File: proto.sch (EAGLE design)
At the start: 2 parts

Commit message: schematic terminada, creo que decente
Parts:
- added JP1, JP2, JP3: (no value), pinhead:PINHD-1X3
- added JP4: (no value), pinhead:PINHD-1X2
- added X1: 87758-1216, con-molex:87758-1216
- added X2: 87758-0416, con-molex:87758-0416
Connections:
- removed net N$8: TB1.VCC, U$1.3.3V
- new net N$12: TB1.A2, X2-2.S
- new net N$13: TB1.B2, X2-4.S
- new net N$14: TB1.B1, X2-3.S
- new net N$15: TB1.A1, X2-1.S
- new net N$17: JP1.2, U$1.A7
- new net N$18: U$1.3.3V, X1-9.S
- new net N$19: U$1.A5, X1-2.S
- new net N$20: U$1.A4, X1-4.S
- new net N$21: U$1.A3, X1-12.S
- new net N$24: U$1.A0, X1-6.S
- new net N$25: JP1.1, JP2.1, JP3.1, JP4.2, TB1.GND2, U$1.GND, X1-1.S
- new net N$26: JP2.2, JP3.2, U$1.A6
- new net N$27: JP1.3, JP2.3, JP3.3, TB1.VCC, U$1.5.5V
- new net N$28: U$1.A2, X1-10.S
- new net N$29: U$1.A1, X1-8.S
- net N$9: now also JP4.1

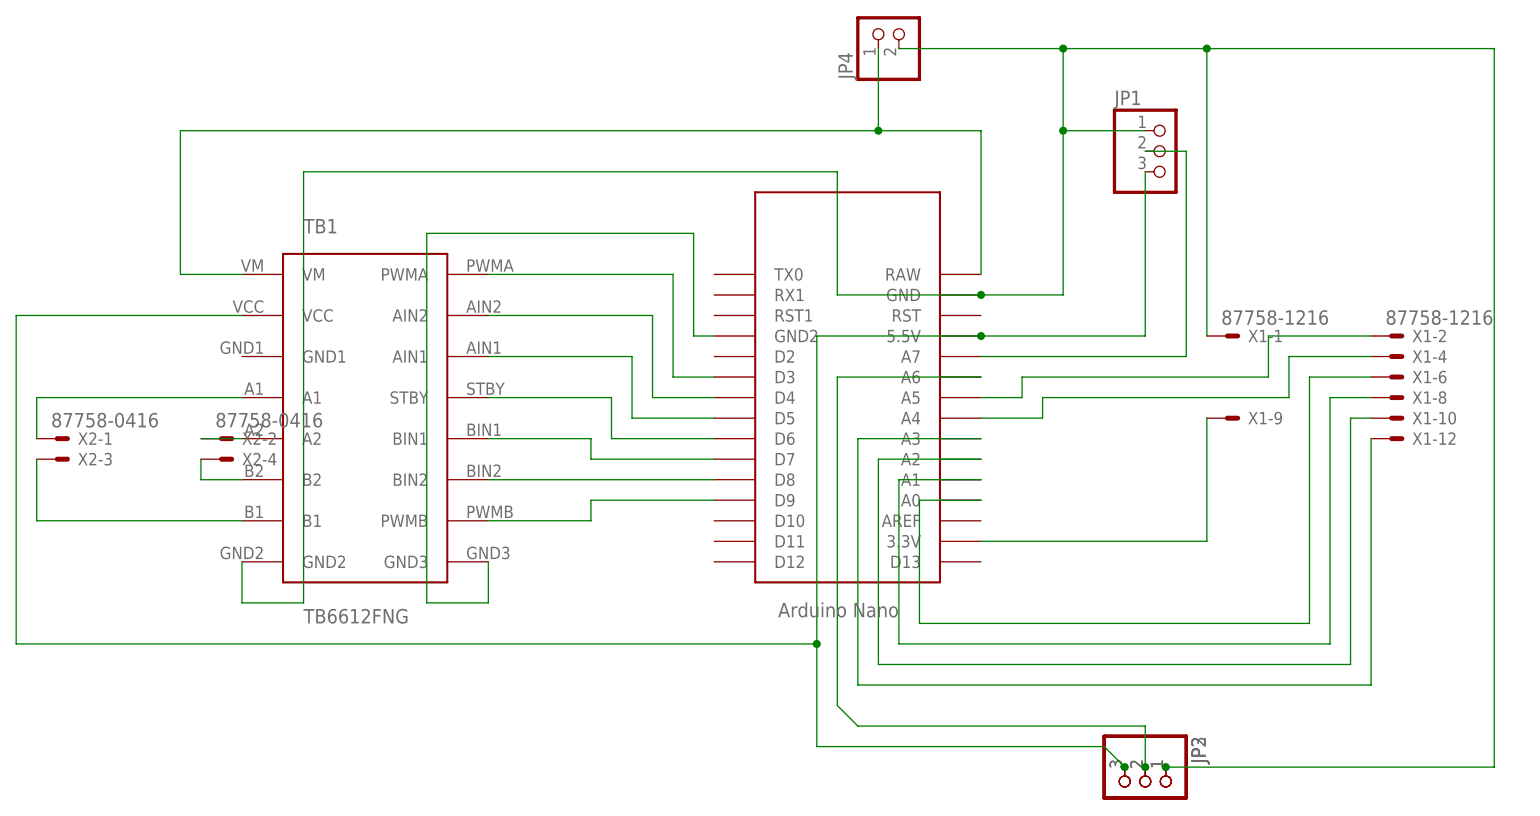
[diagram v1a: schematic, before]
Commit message: finished schematic
last one didn't use the correct pins
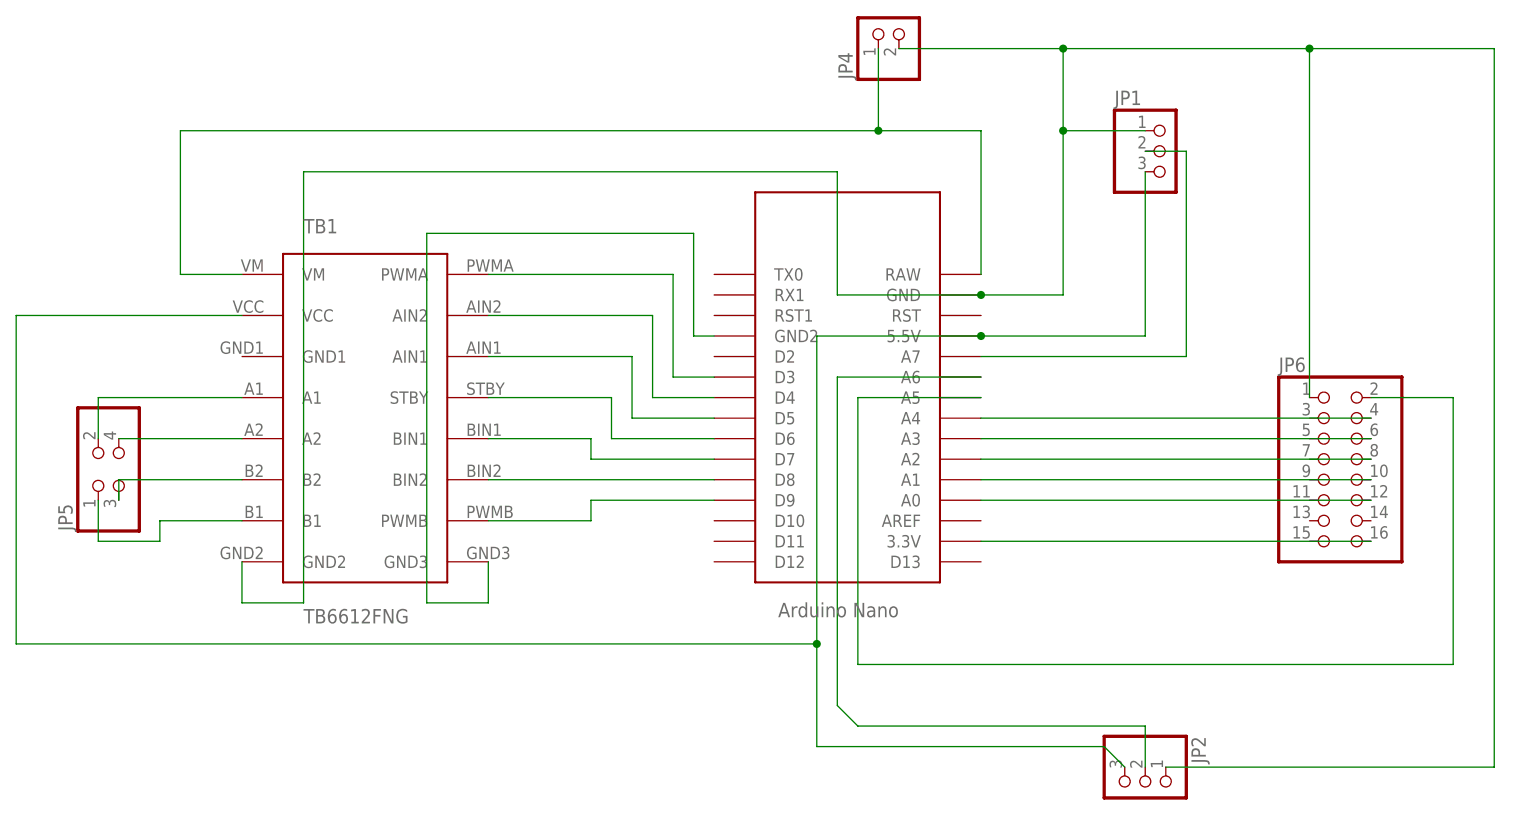
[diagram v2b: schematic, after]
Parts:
- removed JP3: (no value), pinhead:PINHD-1X3
- removed X1: 87758-1216, con-molex:87758-1216
- removed X2: 87758-0416, con-molex:87758-0416
- added JP5: (no value), pinhead:PINHD-2X2
- added JP6: (no value), pinhead:PINHD-2X8
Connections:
- removed net N$24: U$1.A0, X1-6.S
- removed net N$28: U$1.A2, X1-10.S
- removed net N$29: U$1.A1, X1-8.S
- new net N$11: JP5.4, TB1.A2
- new net N$16: JP6.10, U$1.A1
- new net N$8: JP5.2, TB1.A1
- net N$12: now also JP5.3, TB1.B2; no longer TB1.A2, X2-2.S
- net N$13: now also JP5.1, TB1.B1; no longer TB1.B2, X2-4.S
- net N$14: now also JP6.16, U$1.3.3V; no longer TB1.B1, X2-3.S
- net N$15: now also JP6.12, U$1.A0; no longer TB1.A1, X2-1.S
- net N$18: now also JP6.8, U$1.A2; no longer U$1.3.3V, X1-9.S
- net N$19: now also JP6.6, U$1.A3; no longer U$1.A5, X1-2.S
- net N$20: now also JP6.4; no longer X1-4.S
- net N$21: now also JP6.2, U$1.A5; no longer U$1.A3, X1-12.S
- net N$25: now also JP6.1; no longer JP3.1, X1-1.S
- net N$26: no longer JP3.2
- net N$27: no longer JP3.3

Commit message: eliminar tierras
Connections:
- removed net N$10: TB1.GND3, U$1.GND2
- removed net N$25: JP1.1, JP2.1, JP4.2, JP6.1, TB1.GND2, U$1.GND
- net N$14: now also JP6.15
- net N$15: now also JP6.11
- net N$16: now also JP6.9
- net N$18: now also JP6.7
- net N$19: now also JP6.5
- net N$20: now also JP6.3
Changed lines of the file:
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@@
-</segment>
-</net>
-<net name="N$10" class="0">
-<segment>
-<pinref part="U$1" gate="G$1" pin="GND2"/>
-<wire x1="132.08" y1="-22.86" x2="129.54" y2="-22.86" width="0.1524" layer="91"/>
-<wire x1="129.54" y1="-22.86" x2="129.54" y2="-10.16" width="0.1524" layer="91"/>
-<wire x1="129.54" y1="-10.16" x2="96.52" y2="-10.16" width="0.1524" layer="91"/>
-<wire x1="96.52" y1="-10.16" x2="96.52" y2="-55.88" width="0.1524" layer="91"/>
-<wire x1="96.52" y1="-55.88" x2="104.14" y2="-55.88" width="0.1524" layer="91"/>
-<pinref part="TB1" gate="G$1" pin="GND3"/>
-<wire x1="104.14" y1="-55.88" x2="104.14" y2="-50.8" width="0.1524" layer="91"/>
 </segment>
 </net>
@@
 <wire x1="190.5" y1="0" x2="190.5" y2="-25.4" width="0.1524" layer="91"/>
 <wire x1="190.5" y1="-25.4" x2="165.1" y2="-25.4" width="0.1524" layer="91"/>
-</segment>
-</net>
-<net name="N$25" class="0">
-<segment>
-<wire x1="187.96" y1="-76.2" x2="228.6" y2="-76.2" width="0.1524" layer="91"/>
-<pinref part="U$1" gate="G$1" pin="GND"/>
-<wire x1="165.1" y1="-17.78" x2="147.32" y2="-17.78" width="0.1524" layer="91"/>
-<wire x1="147.32" y1="-17.78" x2="147.32" y2="-2.54" width="0.1524" layer="91"/>
-<wire x1="147.32" y1="-2.54" x2="81.28" y2="-2.54" width="0.1524" layer="91"/>
-<wire x1="81.28" y1="-2.54" x2="81.28" y2="-55.88" width="0.1524" layer="91"/>
-<wire x1="81.28" y1="-55.88" x2="73.66" y2="-55.88" width="0.1524" layer="91"/>
-<pinref part="TB1" gate="G$1" pin="GND2"/>
-<wire x1="73.66" y1="-55.88" x2="73.66" y2="-50.8" width="0.1524" layer="91"/>
-<pinref part="JP1" gate="A" pin="1"/>
-<wire x1="185.42" y1="2.54" x2="175.26" y2="2.54" width="0.1524" layer="91"/>
-<wire x1="175.26" y1="2.54" x2="175.26" y2="-17.78" width="0.1524" layer="91"/>
-<wire x1="175.26" y1="-17.78" x2="165.1" y2="-17.78" width="0.1524" layer="91"/>
-<junction x="165.1" y="-17.78"/>
-<wire x1="228.6" y1="-76.2" x2="228.6" y2="12.7" width="0.1524" layer="91"/>
-<wire x1="228.6" y1="12.7" x2="205.74" y2="12.7" width="0.1524" layer="91"/>
-<wire x1="205.74" y1="12.7" x2="175.26" y2="12.7" width="0.1524" layer="91"/>
-<wire x1="175.26" y1="12.7" x2="175.26" y2="2.54" width="0.1524" layer="91"/>
-<junction x="175.26" y="2.54"/>
-<pinref part="JP4" gate="G$1" pin="2"/>
-<wire x1="154.94" y1="12.7" x2="175.26" y2="12.7" width="0.1524" layer="91"/>
-<junction x="175.26" y="12.7"/>
-<pinref part="JP6" gate="A" pin="1"/>
-<wire x1="205.74" y1="-30.48" x2="205.74" y2="12.7" width="0.1524" layer="91"/>
-<junction x="205.74" y="12.7"/>
-<pinref part="JP2" gate="A" pin="1"/>
 </segment>
 </net>
@@
 <pinref part="JP6" gate="A" pin="16"/>
 <pinref part="U$1" gate="G$1" pin="3.3V"/>
-<wire x1="213.36" y1="-48.26" x2="165.1" y2="-48.26" width="0.1524" layer="91"/>
+<wire x1="213.36" y1="-48.26" x2="205.74" y2="-48.26" width="0.1524" layer="91"/>
+<pinref part="JP6" gate="A" pin="15"/>
+<wire x1="205.74" y1="-48.26" x2="165.1" y2="-48.26" width="0.1524" layer="91"/>
+<junction x="205.74" y="-48.26"/>
 </segment>
 </net>
@@
 <pinref part="JP6" gate="A" pin="12"/>
 <pinref part="U$1" gate="G$1" pin="A0"/>
-<wire x1="213.36" y1="-43.18" x2="165.1" y2="-43.18" width="0.1524" layer="91"/>
+<wire x1="213.36" y1="-43.18" x2="205.74" y2="-43.18" width="0.1524" layer="91"/>
+<pinref part="JP6" gate="A" pin="11"/>
+<wire x1="205.74" y1="-43.18" x2="165.1" y2="-43.18" width="0.1524" layer="91"/>
+<junction x="205.74" y="-43.18"/>
 </segment>
 </net>
@@
 <pinref part="JP6" gate="A" pin="10"/>
 <pinref part="U$1" gate="G$1" pin="A1"/>
-<wire x1="213.36" y1="-40.64" x2="165.1" y2="-40.64" width="0.1524" layer="91"/>
+<wire x1="213.36" y1="-40.64" x2="205.74" y2="-40.64" width="0.1524" layer="91"/>
+<pinref part="JP6" gate="A" pin="9"/>
+<wire x1="205.74" y1="-40.64" x2="165.1" y2="-40.64" width="0.1524" layer="91"/>
+<junction x="205.74" y="-40.64"/>
 </segment>
 </net>
@@
 <pinref part="JP6" gate="A" pin="8"/>
 <pinref part="U$1" gate="G$1" pin="A2"/>
-<wire x1="213.36" y1="-38.1" x2="165.1" y2="-38.1" width="0.1524" layer="91"/>
+<wire x1="213.36" y1="-38.1" x2="205.74" y2="-38.1" width="0.1524" layer="91"/>
+<pinref part="JP6" gate="A" pin="7"/>
+<wire x1="205.74" y1="-38.1" x2="165.1" y2="-38.1" width="0.1524" layer="91"/>
+<junction x="205.74" y="-38.1"/>
 </segment>
 </net>
@@
 <pinref part="JP6" gate="A" pin="6"/>
 <pinref part="U$1" gate="G$1" pin="A3"/>
-<wire x1="213.36" y1="-35.56" x2="165.1" y2="-35.56" width="0.1524" layer="91"/>
+<wire x1="213.36" y1="-35.56" x2="205.74" y2="-35.56" width="0.1524" layer="91"/>
+<pinref part="JP6" gate="A" pin="5"/>
+<wire x1="205.74" y1="-35.56" x2="165.1" y2="-35.56" width="0.1524" layer="91"/>
+<junction x="205.74" y="-35.56"/>
 </segment>
 </net>
@@
 <pinref part="JP6" gate="A" pin="4"/>
 <pinref part="U$1" gate="G$1" pin="A4"/>
-<wire x1="213.36" y1="-33.02" x2="165.1" y2="-33.02" width="0.1524" layer="91"/>
+<wire x1="213.36" y1="-33.02" x2="205.74" y2="-33.02" width="0.1524" layer="91"/>
+<pinref part="JP6" gate="A" pin="3"/>
+<wire x1="205.74" y1="-33.02" x2="165.1" y2="-33.02" width="0.1524" layer="91"/>
+<junction x="205.74" y="-33.02"/>
 </segment>
 </net>

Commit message: holi
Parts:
- removed JP6: (no value), pinhead:PINHD-2X8
- added JP3: (no value), pinhead:PINHD-2X9
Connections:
- removed net N$21: JP6.2, U$1.A5
- new net N$10: JP3.4, U$1.A5
- net N$14: now also JP3.6, U$1.A4; no longer JP6.15, JP6.16, U$1.3.3V
- net N$15: now also JP3.8, U$1.A3; no longer JP6.11, JP6.12, U$1.A0
- net N$16: now also JP3.10, U$1.A2; no longer JP6.10, JP6.9, U$1.A1
- net N$18: now also JP3.12, U$1.A1; no longer JP6.7, JP6.8, U$1.A2
- net N$19: now also JP3.14, U$1.A0; no longer JP6.5, JP6.6, U$1.A3
- net N$20: now also JP3.18, U$1.3.3V; no longer JP6.3, JP6.4, U$1.A4
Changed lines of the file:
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@@
 <setting verticaltext="up"/>
 </settings>
-<grid distance="0.1" unitdist="inch" unit="inch" style="lines" multiple="1" display="yes" altdistance="0.01" altunitdist="inch" altunit="inch"/>
+<grid distance="0.1" unitdist="inch" unit="inch" style="lines" multiple="1" display="no" altdistance="0.01" altunitdist="inch" altunit="inch"/>
 <layers>
 <layer number="1" name="Top" color="4" fill="1" visible="no" active="no"/>
@@
 <part name="JP4" library="pinhead" library_urn="urn:adsk.eagle:library:325" deviceset="PINHD-1X2" device="" package3d_urn="urn:adsk.eagle:package:22435/2"/>
 <part name="JP5" library="pinhead" library_urn="urn:adsk.eagle:library:325" deviceset="PINHD-2X2" device="" package3d_urn="urn:adsk.eagle:package:22455/2"/>
-<part name="JP6" library="pinhead" library_urn="urn:adsk.eagle:library:325" deviceset="PINHD-2X8" device="" package3d_urn="urn:adsk.eagle:package:22481/2"/>
 <part name="JP2" library="pinhead" library_urn="urn:adsk.eagle:library:325" deviceset="PINHD-1X3" device="" package3d_urn="urn:adsk.eagle:package:22458/2"/>
+<part name="JP3" library="pinhead" library_urn="urn:adsk.eagle:library:325" deviceset="PINHD-2X9" device="" package3d_urn="urn:adsk.eagle:package:22484/2"/>
 </parts>
 <sheets>
@@
 <attribute name="VALUE" x="63.5" y="-46.99" size="1.778" layer="96" rot="R90"/>
 </instance>
-<instance part="JP6" gate="A" x="208.28" y="-38.1">
-<attribute name="NAME" x="201.93" y="-27.305" size="1.778" layer="95"/>
-<attribute name="VALUE" x="201.93" y="-53.34" size="1.778" layer="96"/>
-</instance>
 <instance part="JP2" gate="A" x="185.42" y="-78.74" rot="R270">
 <attribute name="NAME" x="191.135" y="-72.39" size="1.778" layer="95" rot="R270"/>
 <attribute name="VALUE" x="177.8" y="-72.39" size="1.778" layer="96" rot="R270"/>
+</instance>
+<instance part="JP3" gate="A" x="208.28" y="-38.1">
+<attribute name="NAME" x="201.93" y="-24.765" size="1.778" layer="95"/>
+<attribute name="VALUE" x="201.93" y="-53.34" size="1.778" layer="96"/>
 </instance>
 </instances>
@@
 </segment>
 </net>
+<net name="N$10" class="0">
+<segment>
+<pinref part="U$1" gate="G$1" pin="A5"/>
+<pinref part="JP3" gate="A" pin="4"/>
+<wire x1="165.1" y1="-30.48" x2="213.36" y2="-30.48" width="0.1524" layer="91"/>
+</segment>
+</net>
 <net name="N$14" class="0">
 <segment>
-<pinref part="JP6" gate="A" pin="16"/>
+<pinref part="U$1" gate="G$1" pin="A4"/>
+<pinref part="JP3" gate="A" pin="6"/>
+<wire x1="165.1" y1="-33.02" x2="213.36" y2="-33.02" width="0.1524" layer="91"/>
+</segment>
+</net>
+<net name="N$15" class="0">
+<segment>
+<pinref part="U$1" gate="G$1" pin="A3"/>
+<pinref part="JP3" gate="A" pin="8"/>
+<wire x1="165.1" y1="-35.56" x2="213.36" y2="-35.56" width="0.1524" layer="91"/>
+</segment>
+</net>
+<net name="N$16" class="0">
+<segment>
+<pinref part="JP3" gate="A" pin="10"/>
+<pinref part="U$1" gate="G$1" pin="A2"/>
+<wire x1="213.36" y1="-38.1" x2="165.1" y2="-38.1" width="0.1524" layer="91"/>
+</segment>
+</net>
+<net name="N$18" class="0">
+<segment>
+<pinref part="U$1" gate="G$1" pin="A1"/>
+<pinref part="JP3" gate="A" pin="12"/>
+<wire x1="165.1" y1="-40.64" x2="213.36" y2="-40.64" width="0.1524" layer="91"/>
+</segment>
+</net>
+<net name="N$19" class="0">
+<segment>
+<pinref part="JP3" gate="A" pin="14"/>
+<pinref part="U$1" gate="G$1" pin="A0"/>
+<wire x1="213.36" y1="-43.18" x2="165.1" y2="-43.18" width="0.1524" layer="91"/>
+</segment>
+</net>
+<net name="N$20" class="0">
+<segment>
 <pinref part="U$1" gate="G$1" pin="3.3V"/>
-<wire x1="213.36" y1="-48.26" x2="205.74" y2="-48.26" width="0.1524" layer="91"/>
-<pinref part="JP6" gate="A" pin="15"/>
-<wire x1="205.74" y1="-48.26" x2="165.1" y2="-48.26" width="0.1524" layer="91"/>
-<junction x="205.74" y="-48.26"/>
-</segment>
-</net>
-<net name="N$15" class="0">
-<segment>
-<pinref part="JP6" gate="A" pin="12"/>
-<pinref part="U$1" gate="G$1" pin="A0"/>
-<wire x1="213.36" y1="-43.18" x2="205.74" y2="-43.18" width="0.1524" layer="91"/>
-<pinref part="JP6" gate="A" pin="11"/>
-<wire x1="205.74" y1="-43.18" x2="165.1" y2="-43.18" width="0.1524" layer="91"/>
-<junction x="205.74" y="-43.18"/>
-</segment>
-</net>
-<net name="N$16" class="0">
-<segment>
-<pinref part="JP6" gate="A" pin="10"/>
-<pinref part="U$1" gate="G$1" pin="A1"/>
-<wire x1="213.36" y1="-40.64" x2="205.74" y2="-40.64" width="0.1524" layer="91"/>
-<pinref part="JP6" gate="A" pin="9"/>
-<wire x1="205.74" y1="-40.64" x2="165.1" y2="-40.64" width="0.1524" layer="91"/>
-<junction x="205.74" y="-40.64"/>
-</segment>
-</net>
-<net name="N$18" class="0">
-<segment>
-<pinref part="JP6" gate="A" pin="8"/>
-<pinref part="U$1" gate="G$1" pin="A2"/>
-<wire x1="213.36" y1="-38.1" x2="205.74" y2="-38.1" width="0.1524" layer="91"/>
-<pinref part="JP6" gate="A" pin="7"/>
-<wire x1="205.74" y1="-38.1" x2="165.1" y2="-38.1" width="0.1524" layer="91"/>
-<junction x="205.74" y="-38.1"/>
-</segment>
-</net>
-<net name="N$19" class="0">
-<segment>
-<pinref part="JP6" gate="A" pin="6"/>
-<pinref part="U$1" gate="G$1" pin="A3"/>
-<wire x1="213.36" y1="-35.56" x2="205.74" y2="-35.56" width="0.1524" layer="91"/>
-<pinref part="JP6" gate="A" pin="5"/>
-<wire x1="205.74" y1="-35.56" x2="165.1" y2="-35.56" width="0.1524" layer="91"/>
-<junction x="205.74" y="-35.56"/>
-</segment>
-</net>
-<net name="N$20" class="0">
-<segment>
-<pinref part="JP6" gate="A" pin="4"/>
-<pinref part="U$1" gate="G$1" pin="A4"/>
-<wire x1="213.36" y1="-33.02" x2="205.74" y2="-33.02" width="0.1524" layer="91"/>
-<pinref part="JP6" gate="A" pin="3"/>
-<wire x1="205.74" y1="-33.02" x2="165.1" y2="-33.02" width="0.1524" layer="91"/>
-<junction x="205.74" y="-33.02"/>
-</segment>
-</net>
-<net name="N$21" class="0">
-<segment>
-<pinref part="JP6" gate="A" pin="2"/>
-<wire x1="213.36" y1="-30.48" x2="223.52" y2="-30.48" width="0.1524" layer="91"/>
-<wire x1="223.52" y1="-30.48" x2="223.52" y2="-63.5" width="0.1524" layer="91"/>
-<wire x1="223.52" y1="-63.5" x2="149.86" y2="-63.5" width="0.1524" layer="91"/>
-<wire x1="149.86" y1="-63.5" x2="149.86" y2="-30.48" width="0.1524" layer="91"/>
-<pinref part="U$1" gate="G$1" pin="A5"/>
-<wire x1="149.86" y1="-30.48" x2="165.1" y2="-30.48" width="0.1524" layer="91"/>
-</segment>
-</net>
+<pinref part="JP3" gate="A" pin="18"/>
+<wire x1="165.1" y1="-48.26" x2="213.36" y2="-48.26" width="0.1524" layer="91"/>
+</segment>
+</net>

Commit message: monton de weas
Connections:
- new net GND: JP1.1, JP2.1, JP3.1, JP4.2, TB1.GND2, TB1.GND3, U$1.GND, U$1.GND2
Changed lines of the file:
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@@
+</segment>
+</net>
+<net name="GND" class="0">
+<segment>
+<pinref part="TB1" gate="G$1" pin="GND2"/>
+<wire x1="73.66" y1="-50.8" x2="73.66" y2="-55.88" width="0.1524" layer="91"/>
+<wire x1="73.66" y1="-55.88" x2="66.04" y2="-55.88" width="0.1524" layer="91"/>
+</segment>
+<segment>
+<pinref part="TB1" gate="G$1" pin="GND3"/>
+<wire x1="104.14" y1="-50.8" x2="111.76" y2="-50.8" width="0.1524" layer="91"/>
+<wire x1="111.76" y1="-50.8" x2="111.76" y2="-53.34" width="0.1524" layer="91"/>
+<label x="71.12" y="-55.88" size="1.778" layer="95"/>
+</segment>
+<segment>
+<pinref part="U$1" gate="G$1" pin="GND"/>
+<wire x1="165.1" y1="-17.78" x2="177.8" y2="-17.78" width="0.1524" layer="91"/>
+<label x="132.08" y="-22.86" size="1.778" layer="95"/>
+</segment>
+<segment>
+<pinref part="U$1" gate="G$1" pin="GND2"/>
+<wire x1="132.08" y1="-22.86" x2="129.54" y2="-22.86" width="0.1524" layer="91"/>
+<label x="187.96" y="-68.58" size="1.778" layer="95"/>
+</segment>
+<segment>
+<pinref part="JP2" gate="A" pin="1"/>
+<wire x1="187.96" y1="-76.2" x2="187.96" y2="-68.58" width="0.1524" layer="91"/>
+<label x="154.94" y="7.62" size="1.778" layer="95"/>
+</segment>
+<segment>
+<pinref part="JP4" gate="G$1" pin="2"/>
+<wire x1="154.94" y1="12.7" x2="154.94" y2="7.62" width="0.1524" layer="91"/>
+<wire x1="154.94" y1="7.62" x2="157.48" y2="7.62" width="0.1524" layer="91"/>
+<label x="182.88" y="2.54" size="1.778" layer="95"/>
+</segment>
+<segment>
+<pinref part="JP1" gate="A" pin="1"/>
+<wire x1="185.42" y1="2.54" x2="177.8" y2="2.54" width="0.1524" layer="91"/>
+<label x="200.66" y="-27.94" size="1.778" layer="95"/>
+</segment>
+<segment>
+<pinref part="JP3" gate="A" pin="1"/>
+<wire x1="205.74" y1="-27.94" x2="195.58" y2="-27.94" width="0.1524" layer="91"/>
+<label x="109.22" y="-50.8" size="1.778" layer="95"/>
 </segment>
 </net>
